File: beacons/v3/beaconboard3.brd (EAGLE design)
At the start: 143.5 x 76.2 mm, 46 parts, among them IC1 7805TV, Q1 2N3904, Q2 16MHz, Q3 2N3904, Q4 2N3904, Q5 2N3904

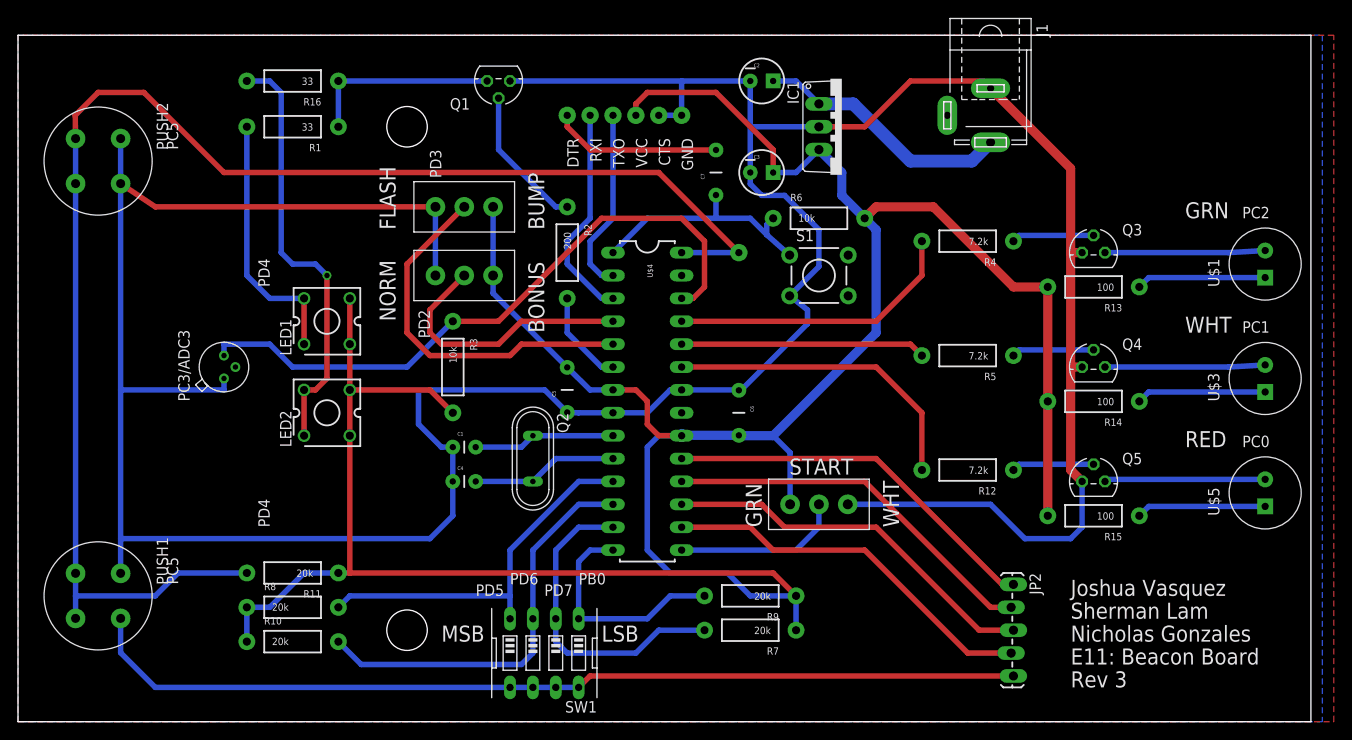
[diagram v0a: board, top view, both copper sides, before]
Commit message: Updated readme. Added omron switches in version 3
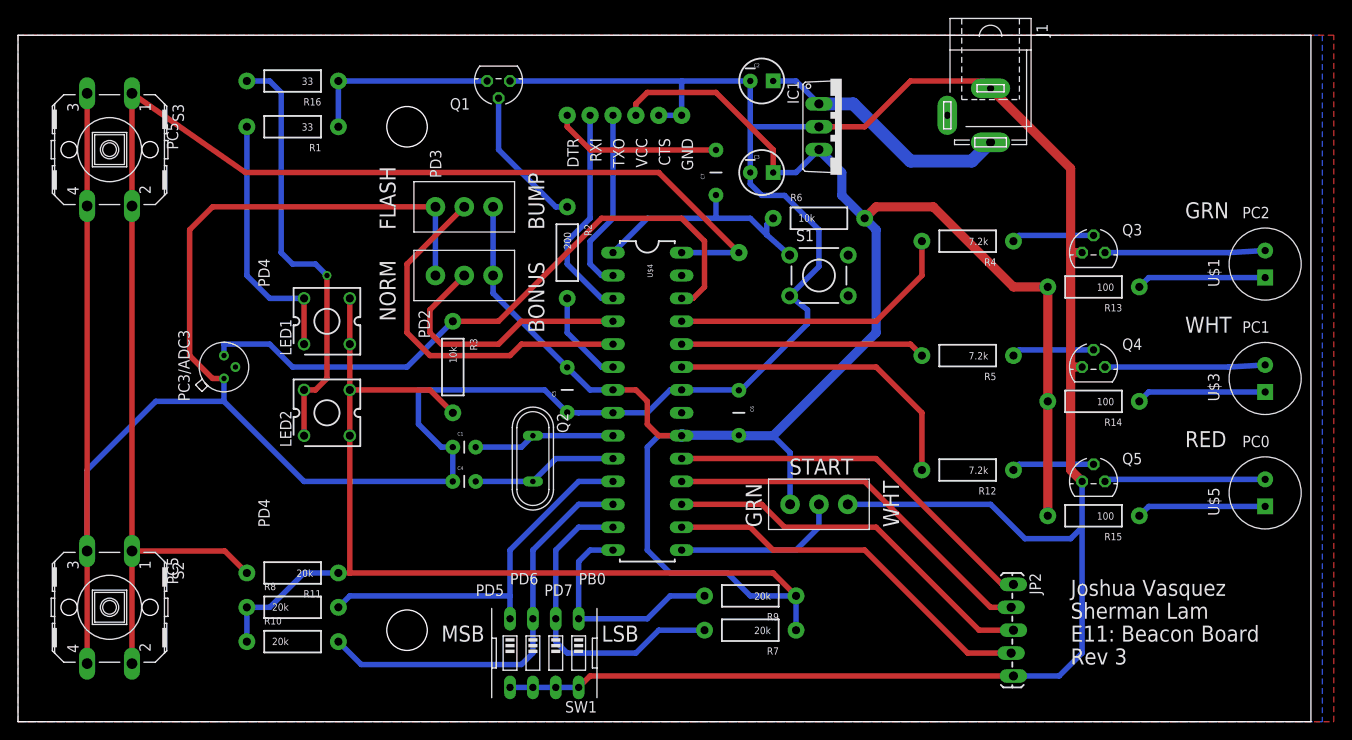
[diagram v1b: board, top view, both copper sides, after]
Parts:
- removed PUSH1, PUSH2: D6_PUSHBUTTON, e11:D6_PUSH_BUTTON
- added S2, S3: (no value), switch-omron:B3F-40XX
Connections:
- net BUMPER: now also S2.1, S2.2, S3.1, S3.2; no longer PUSH1.3, PUSH1.4, PUSH2.3, PUSH2.4
- net GND: now also S2.3, S2.4, S3.3, S3.4; no longer PUSH1.1, PUSH1.2, PUSH2.1, PUSH2.2
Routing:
- net BUMPER: track 164.3 -> 157.2 mm
- net GND: track 491.6 -> 497.4 mm
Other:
- board text removed: "Nicholas Gonzales"
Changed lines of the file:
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@@
 <wire x1="146.05" y1="76.2" x2="2.54" y2="76.2" width="0" layer="20"/>
 <wire x1="2.54" y1="76.2" x2="2.54" y2="0" width="0" layer="20"/>
-<text x="119.38" y="6.35" size="1.778" layer="25" rot="SR0">E11: Beacon Board</text>
+<text x="119.38" y="8.89" size="1.778" layer="25" rot="SR0">E11: Beacon Board</text>
 <text x="119.38" y="13.97" size="1.778" layer="25" rot="SR0">Joshua Vasquez</text>
-<text x="119.38" y="3.81" size="1.778" layer="25" rot="SR0">Rev 3</text>
+<text x="119.38" y="6.35" size="1.778" layer="25" rot="SR0">Rev 3</text>
 <text x="119.38" y="11.43" size="1.778" layer="25" rot="SR0">Sherman Lam</text>
-<text x="119.38" y="8.89" size="1.778" layer="25" rot="SR0">Nicholas Gonzales</text>
 <hole x="45.72" y="10.16" drill="4.4958"/>
 <hole x="45.72" y="66.04" drill="4.4958"/>
@@
 <element name="JP2" library="SparkFun-Connectors" package="1X05_LOCK_LONGPADS" value="" x="113.03" y="15.24" rot="R270"/>
 <element name="R11" library="SparkFun-Resistors" package="AXIAL-0.4" value="20k" x="33.02" y="16.51" rot="R180"/>
-<element name="PUSH1" library="e11" package="D6_PUSH_BUTTON" value="D6_PUSHBUTTON" x="11.43" y="13.97" rot="R270"/>
-<element name="PUSH2" library="e11" package="D6_PUSH_BUTTON" value="D6_PUSHBUTTON" x="11.43" y="62.23" rot="R270"/>
 <element name="U$2" library="e11" package="TO-18" value="BPW77NA" x="25.4" y="39.37" rot="R90"/>
 <element name="R3" library="SparkFun-Resistors" package="AXIAL-0.4" value="10k" x="50.8" y="39.37" rot="R270"/>
@@
 <element name="R16" library="SparkFun-Resistors" package="AXIAL-0.4" value="33" x="33.02" y="71.12" rot="R180"/>
 <element name="MODE3" library="e11" package="SPDT_SLIDE_SWITCH" value="SPD_SLIDE_SWITCH" x="91.44" y="24.13"/>
+<element name="S2" library="switch-omron" package="B3F-40XX" value="" x="12.7" y="12.7" rot="R270">
+<attribute name="OC_NEWARK" value="36K3105" x="12.7" y="12.7" size="1.778" layer="27" rot="R270" display="off"/>
+<attribute name="MPN" value="B3F-4000" x="12.7" y="12.7" size="1.778" layer="27" rot="R270" display="off"/>
+<attribute name="MF" value="OMRON COMPONENTS USA" x="12.7" y="12.7" size="1.778" layer="27" rot="R270" display="off"/>
+<attribute name="OC_FARNELL" value="176434" x="12.7" y="12.7" size="1.778" layer="27" rot="R270" display="off"/>
+</element>
+<element name="S3" library="switch-omron" package="B3F-40XX" value="" x="12.7" y="63.5" rot="R270">
+<attribute name="OC_NEWARK" value="36K3105" x="12.7" y="63.5" size="1.778" layer="27" rot="R270" display="off"/>
+<attribute name="MPN" value="B3F-4000" x="12.7" y="63.5" size="1.778" layer="27" rot="R270" display="off"/>
+<attribute name="MF" value="OMRON COMPONENTS USA" x="12.7" y="63.5" size="1.778" layer="27" rot="R270" display="off"/>
+<attribute name="OC_FARNELL" value="176434" x="12.7" y="63.5" size="1.778" layer="27" rot="R270" display="off"/>
+</element>
 </elements>
 <signals>
@@
 <contactref element="Q1" pad="E"/>
 <contactref element="J1" pad="1"/>
-<contactref element="PUSH1" pad="2"/>
-<contactref element="PUSH1" pad="1"/>
-<contactref element="PUSH2" pad="2"/>
-<contactref element="PUSH2" pad="1"/>
-<wire x1="13.93" y1="11.47" x2="13.93" y2="7.66" width="0.6096" layer="16"/>
-<wire x1="13.93" y1="7.66" x2="17.78" y2="3.81" width="0.6096" layer="16"/>
-<wire x1="17.78" y1="3.81" x2="57.15" y2="3.81" width="0.6096" layer="16"/>
-<wire x1="13.93" y1="16.47" x2="13.93" y2="20.32" width="0.6096" layer="16"/>
-<wire x1="13.93" y1="20.32" x2="13.93" y2="36.83" width="0.6096" layer="16"/>
-<wire x1="13.93" y1="36.83" x2="13.93" y2="59.73" width="0.6096" layer="16"/>
-<wire x1="13.93" y1="59.73" x2="13.93" y2="64.73" width="0.6096" layer="16"/>
-<wire x1="50.8" y1="26.67" x2="50.8" y2="22.86" width="0.6096" layer="16"/>
-<wire x1="50.8" y1="22.86" x2="48.26" y2="20.32" width="0.6096" layer="16"/>
-<wire x1="48.26" y1="20.32" x2="13.93" y2="20.32" width="0.6096" layer="16"/>
 <contactref element="U$2" pad="E"/>
 <contactref element="MODE1" pad="3"/>
@@
 <wire x1="119.38" y1="52.07" x2="119.38" y2="61.42" width="1.016" layer="1"/>
 <wire x1="120.65" y1="39.37" x2="119.38" y2="39.37" width="1.016" layer="1"/>
-<wire x1="25.4" y1="36.83" x2="25.4" y2="38.1" width="0.6096" layer="16"/>
 <wire x1="91.44" y1="66.04" x2="96.52" y2="66.04" width="0.6096" layer="1"/>
 <wire x1="96.52" y1="66.04" x2="101.6" y2="71.12" width="0.6096" layer="1"/>
 <wire x1="101.6" y1="71.12" x2="109.68" y2="71.12" width="0.6096" layer="1"/>
 <wire x1="109.68" y1="71.12" x2="110.49" y2="70.31" width="0.6096" layer="1"/>
-<wire x1="48.8696" y1="57.15" x2="48.8696" y2="49.53" width="0.6096" layer="16"/>
 <wire x1="57.15" y1="71.12" x2="76.2" y2="71.12" width="0.6096" layer="16"/>
 <wire x1="76.2" y1="71.12" x2="83.82" y2="71.12" width="0.6096" layer="16"/>
@@
 <wire x1="91.44" y1="54.61" x2="91.44" y2="50.5206" width="0.6096" layer="16"/>
 <wire x1="91.44" y1="50.5206" x2="88.1888" y2="47.2694" width="0.6096" layer="16"/>
-<wire x1="48.8696" y1="57.15" x2="17.78" y2="57.15" width="0.6096" layer="1"/>
-<wire x1="17.78" y1="57.15" x2="13.93" y2="59.73" width="0.6096" layer="1"/>
 <wire x1="46.99" y1="36.83" x2="61" y2="36.83" width="0.6096" layer="16"/>
 <wire x1="61" y1="36.83" x2="63.5" y2="34.33" width="0.6096" layer="16"/>
@@
 <wire x1="49.53" y1="30.48" x2="46.99" y2="33.02" width="0.6096" layer="16"/>
 <wire x1="46.99" y1="33.02" x2="46.99" y2="36.83" width="0.6096" layer="16"/>
-<wire x1="25.4" y1="36.83" x2="13.93" y2="36.83" width="0.6096" layer="16"/>
 <contactref element="MODE3" pad="3"/>
 <wire x1="94.6404" y1="24.13" x2="110.49" y2="24.13" width="0.6096" layer="16"/>
@@
 <wire x1="113.03" y1="5.08" x2="66.04" y2="5.08" width="0.6096" layer="1"/>
 <wire x1="66.04" y1="5.08" x2="64.77" y2="3.81" width="0.6096" layer="1"/>
-<wire x1="13.93" y1="11.47" x2="13.93" y2="16.47" width="0" layer="19" extent="1-1"/>
+<contactref element="S3" pad="3"/>
+<contactref element="S3" pad="4"/>
+<contactref element="S2" pad="3"/>
+<contactref element="S2" pad="4"/>
+<wire x1="10.2108" y1="69.7484" x2="10.2108" y2="57.2516" width="0.6096" layer="1"/>
+<wire x1="10.2108" y1="6.4516" x2="10.2108" y2="18.9484" width="0.6096" layer="1"/>
+<wire x1="10.2108" y1="18.9484" x2="10.2108" y2="57.2516" width="0.6096" layer="1"/>
+<wire x1="25.4" y1="38.1" x2="25.4" y2="35.56" width="0.6096" layer="16"/>
+<wire x1="25.4" y1="35.56" x2="34.29" y2="26.67" width="0.6096" layer="16"/>
+<wire x1="34.29" y1="26.67" x2="50.8" y2="26.67" width="0.6096" layer="16"/>
+<wire x1="25.4" y1="35.56" x2="17.8308" y2="35.56" width="0.6096" layer="16"/>
+<wire x1="17.8308" y1="35.56" x2="10.2108" y2="27.94" width="0.6096" layer="16"/>
+<wire x1="10.2108" y1="27.94" x2="10.2108" y2="18.9484" width="0.6096" layer="16"/>
+<wire x1="48.8696" y1="57.15" x2="24.13" y2="57.15" width="0.6096" layer="1"/>
+<wire x1="24.13" y1="57.15" x2="21.59" y2="54.61" width="0.6096" layer="1"/>
+<wire x1="21.59" y1="54.61" x2="21.59" y2="40.64" width="0.6096" layer="1"/>
+<wire x1="21.59" y1="40.64" x2="24.13" y2="38.1" width="0.6096" layer="1"/>
+<wire x1="24.13" y1="38.1" x2="25.4" y2="38.1" width="0.6096" layer="1"/>
+<wire x1="48.8696" y1="49.53" x2="48.8696" y2="56.5404" width="0.6096" layer="16"/>
+<wire x1="48.8696" y1="56.5404" x2="48.26" y2="57.15" width="0.6096" layer="16"/>
+<wire x1="48.26" y1="57.15" x2="48.8696" y2="57.15" width="0.6096" layer="16"/>
+<wire x1="113.03" y1="5.08" x2="118.11" y2="5.08" width="0.6096" layer="16"/>
+<wire x1="118.11" y1="5.08" x2="120.65" y2="7.62" width="0.6096" layer="16"/>
+<wire x1="120.65" y1="7.62" x2="120.65" y2="21.59" width="0.6096" layer="16"/>
 </signal>
 <signal name="VDD">
@@
 <via x="82.55" y="52.07" extent="1-16" drill="0.8" diameter="1.9304" shape="square"/>
 <wire x1="82.55" y1="52.07" x2="73.66" y2="60.96" width="0.6096" layer="1"/>
-<contactref element="PUSH1" pad="4"/>
-<contactref element="PUSH1" pad="3"/>
 <contactref element="R11" pad="P$2"/>
-<contactref element="PUSH2" pad="4"/>
-<contactref element="PUSH2" pad="3"/>
-<wire x1="8.93" y1="11.47" x2="8.93" y2="13.97" width="0.6096" layer="16"/>
-<wire x1="8.93" y1="13.97" x2="8.93" y2="16.47" width="0.6096" layer="16"/>
-<wire x1="8.93" y1="16.47" x2="8.93" y2="59.73" width="0.6096" layer="16"/>
-<wire x1="8.93" y1="59.73" x2="8.93" y2="64.73" width="0.6096" layer="16"/>
-<wire x1="27.94" y1="16.51" x2="20.32" y2="16.51" width="0.6096" layer="16"/>
-<wire x1="20.32" y1="16.51" x2="17.78" y2="13.97" width="0.6096" layer="16"/>
-<wire x1="17.78" y1="13.97" x2="8.93" y2="13.97" width="0.6096" layer="16"/>
-<wire x1="73.66" y1="60.96" x2="25.4" y2="60.96" width="0.6096" layer="1"/>
-<wire x1="25.4" y1="60.96" x2="16.51" y2="69.85" width="0.6096" layer="1"/>
-<wire x1="16.51" y1="69.85" x2="11.43" y2="69.85" width="0.6096" layer="1"/>
-<wire x1="11.43" y1="69.85" x2="8.89" y2="67.31" width="0.6096" layer="1"/>
-<wire x1="8.89" y1="67.31" x2="8.93" y2="64.73" width="0.6096" layer="1"/>
+<contactref element="S3" pad="1"/>
+<contactref element="S3" pad="2"/>
+<contactref element="S2" pad="1"/>
+<contactref element="S2" pad="2"/>
+<wire x1="73.66" y1="60.96" x2="27.7876" y2="60.96" width="0.6096" layer="1"/>
+<wire x1="27.7876" y1="60.96" x2="15.1892" y2="69.7484" width="0.6096" layer="1"/>
+<wire x1="15.1892" y1="57.2516" x2="15.1892" y2="69.7484" width="0.6096" layer="1"/>
+<wire x1="15.1892" y1="57.2516" x2="15.1892" y2="18.9484" width="0.6096" layer="1"/>
+<wire x1="15.1892" y1="18.9484" x2="25.5016" y2="18.9484" width="0.6096" layer="1"/>
+<wire x1="25.5016" y1="18.9484" x2="27.94" y2="16.51" width="0.6096" layer="1"/>
+<wire x1="15.1892" y1="6.4516" x2="15.1892" y2="18.9484" width="0.6096" layer="1"/>
 </signal>
 <signal name="N$9">

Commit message: Added pdf of sch and updated boms
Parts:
- renumbered LED2 to HF5-R5590, S2 to B3F-4050
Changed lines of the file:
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@@
 <element name="C3" library="SparkFun-Capacitors" package="CPOL-RADIAL-10UF-25V" value="47uF" x="85.09" y="60.96"/>
 <element name="LED1" library="led" package="CP41B" value="" x="36.83" y="44.45" rot="R90"/>
-<element name="LED2" library="led" package="CP41B" value="" x="36.83" y="34.29" rot="R90"/>
+<element name="HF5-R5590" library="led" package="CP41B" value="" x="36.83" y="34.29" rot="R90"/>
 <element name="R1" library="SparkFun-Resistors" package="AXIAL-0.4" value="33" x="33.02" y="66.04" rot="R180"/>
 <element name="R2" library="SparkFun-Resistors" package="AXIAL-0.4" value="200" x="63.5" y="52.07" rot="R270"/>
@@
 <element name="R16" library="SparkFun-Resistors" package="AXIAL-0.4" value="33" x="33.02" y="71.12" rot="R180"/>
 <element name="MODE3" library="e11" package="SPDT_SLIDE_SWITCH" value="SPD_SLIDE_SWITCH" x="91.44" y="24.13"/>
-<element name="S2" library="switch-omron" package="B3F-40XX" value="" x="12.7" y="12.7" rot="R270">
+<element name="B3F-4050" library="switch-omron" package="B3F-40XX" value="" x="12.7" y="12.7" rot="R270">
 <attribute name="OC_NEWARK" value="36K3105" x="12.7" y="12.7" size="1.778" layer="27" rot="R270" display="off"/>
 <attribute name="MPN" value="B3F-4000" x="12.7" y="12.7" size="1.778" layer="27" rot="R270" display="off"/>
@@
 <contactref element="LED1" pad="2"/>
 <contactref element="LED1" pad="3"/>
-<contactref element="LED2" pad="2"/>
-<contactref element="LED2" pad="3"/>
+<contactref element="HF5-R5590" pad="2"/>
+<contactref element="HF5-R5590" pad="3"/>
 <wire x1="39.37" y1="36.83" x2="39.37" y2="41.91" width="0.6096" layer="1"/>
 <contactref element="R3" pad="P$2"/>
@@
 <contactref element="S3" pad="3"/>
 <contactref element="S3" pad="4"/>
-<contactref element="S2" pad="3"/>
-<contactref element="S2" pad="4"/>
+<contactref element="B3F-4050" pad="3"/>
+<contactref element="B3F-4050" pad="4"/>
 <wire x1="10.2108" y1="69.7484" x2="10.2108" y2="57.2516" width="0.6096" layer="1"/>
 <wire x1="10.2108" y1="6.4516" x2="10.2108" y2="18.9484" width="0.6096" layer="1"/>
@@
 <contactref element="S3" pad="1"/>
 <contactref element="S3" pad="2"/>
-<contactref element="S2" pad="1"/>
-<contactref element="S2" pad="2"/>
+<contactref element="B3F-4050" pad="1"/>
+<contactref element="B3F-4050" pad="2"/>
 <wire x1="73.66" y1="60.96" x2="27.7876" y2="60.96" width="0.6096" layer="1"/>
 <wire x1="27.7876" y1="60.96" x2="15.1892" y2="69.7484" width="0.6096" layer="1"/>
@@
 <signal name="N$25">
 <contactref element="R16" pad="P$2"/>
-<contactref element="LED2" pad="4"/>
-<contactref element="LED2" pad="1"/>
+<contactref element="HF5-R5590" pad="4"/>
+<contactref element="HF5-R5590" pad="1"/>
 <wire x1="27.94" y1="71.12" x2="30.48" y2="71.12" width="0.6096" layer="16"/>
 <wire x1="30.48" y1="71.12" x2="31.75" y2="69.85" width="0.6096" layer="16"/>
